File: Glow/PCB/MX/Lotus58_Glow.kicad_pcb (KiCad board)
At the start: 2 copper layers, 139.1 x 107.7 mm, 122 parts, among them J1 AudioJack4, P4 OLED, SW1 SW_PUSH, SW10 SW_PUSH, SW11 SW_PUSH, SW12 SW_PUSH, SW13 SW_PUSH, SW14 SW_PUSH, SW15 SW_PUSH, SW16 SW_PUSH, SW17 SW_PUSH, SW18 SW_PUSH, SW19 SW_PUSH, SW2 SW_PUSH, SW20 SW_PUSH, SW21 SW_PUSH, SW22 SW_PUSH, SW23 SW_PUSH, SW24 SW_PUSH, SW25 SW_PUSH, SW26 SW_PUSH, SW27 SW_PUSH, SW28 SW_PUSH, SW29 SW_PUSH, SW3 SW_PUSH, SW30 Rotary_Encoder_Switch, SW31 Rotary_Encoder_Switch, SW4 SW_PUSH, SW5 SW_PUSH, SW6 SW_PUSH, SW7 SW_PUSH, SW8 SW_PUSH, SW9 SW_PUSH, U1 ProMicro

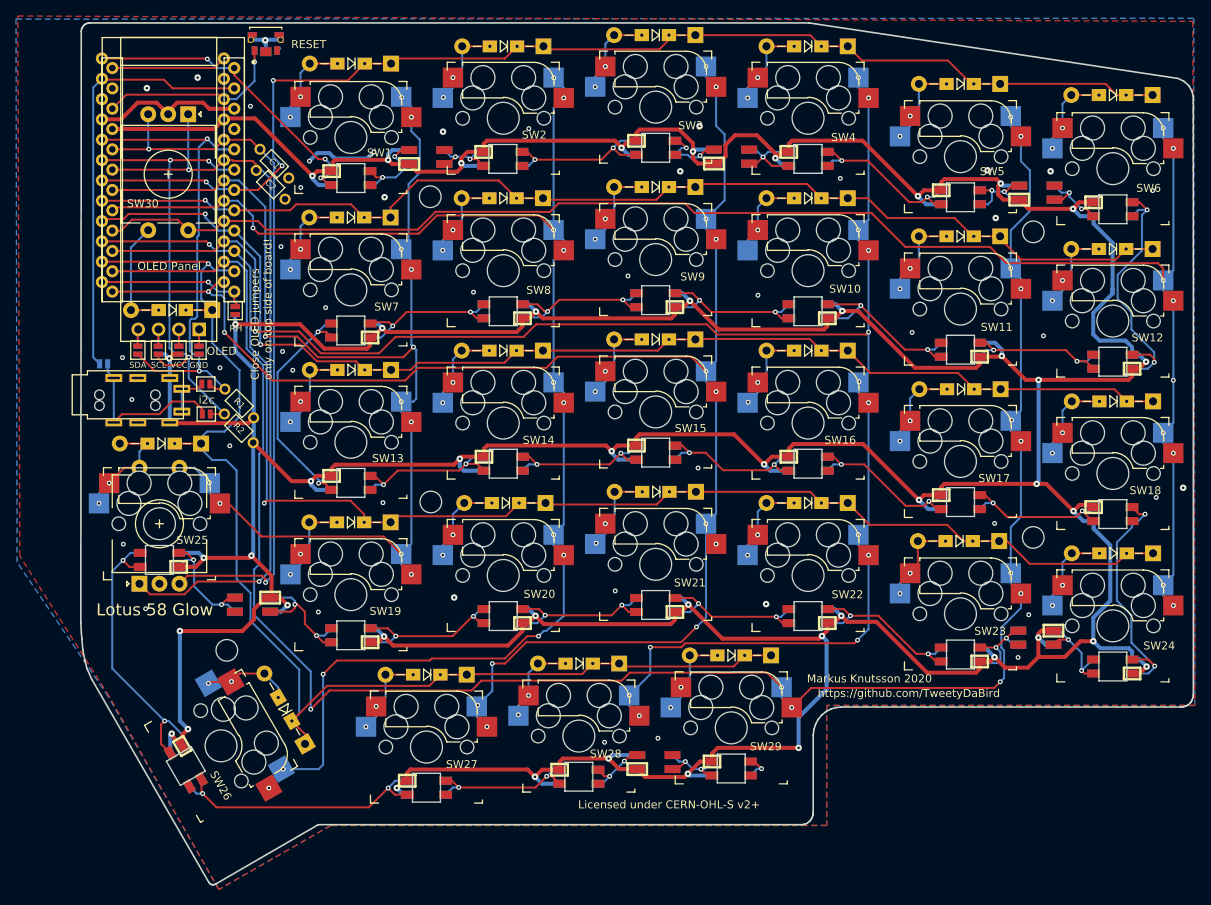
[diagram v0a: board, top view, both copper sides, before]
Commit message: RGB midmount footprints
Fixed mirror image pinout
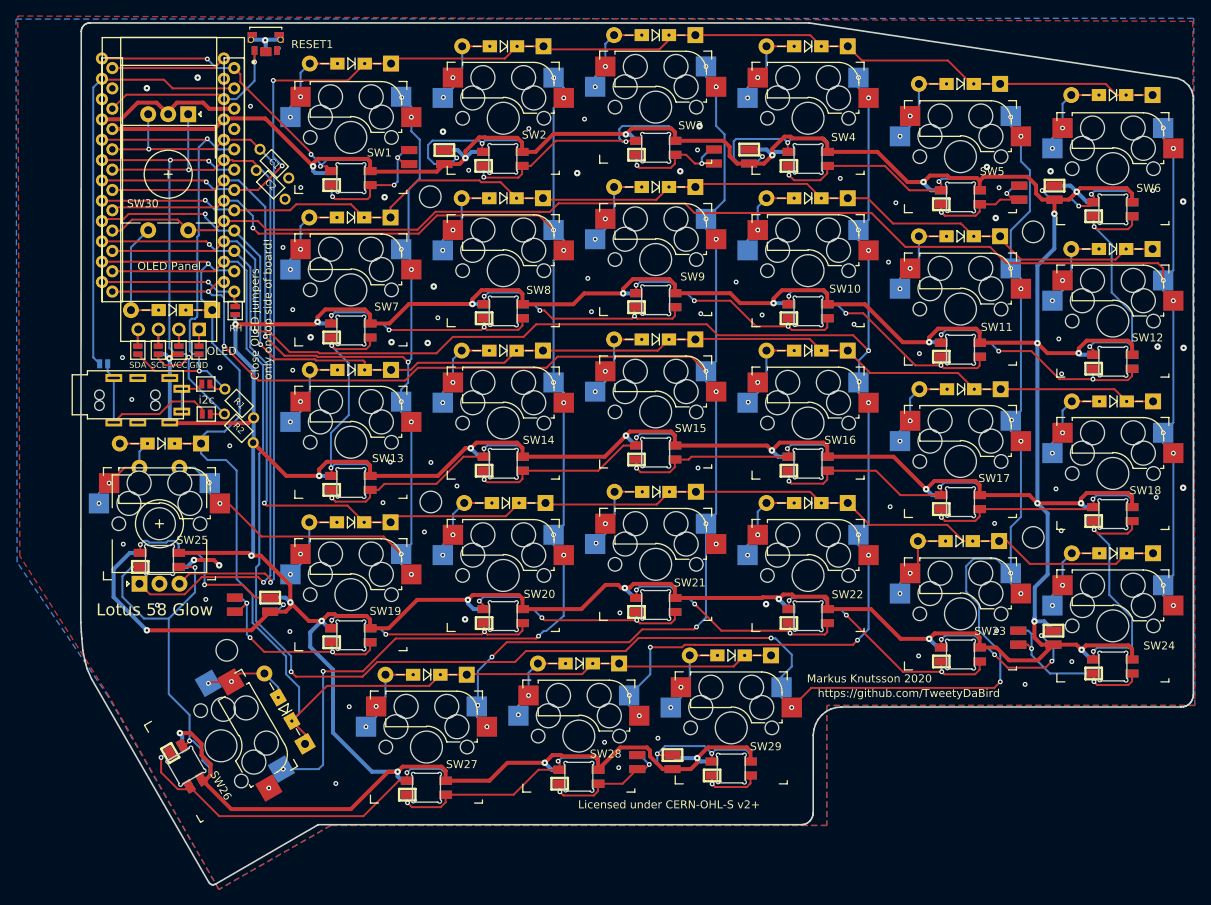
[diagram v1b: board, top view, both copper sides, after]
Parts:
- turned L1 to 0 degrees
- turned L13 to 0 degrees
- turned L14 to 0 degrees
- turned L15 to 0 degrees
- turned L16 to 0 degrees
- turned L17 to 0 degrees
- turned L18 to 0 degrees
- turned L26 to 300 degrees
- turned L27 to 0 degrees
- turned L28 to 0 degrees
- turned L29 to 0 degrees
- turned L3 to 0 degrees
- turned L31 to 0 degrees
- turned L33 to 0 degrees
- turned L34 to 0 degrees
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- renumbered RESET to RESET1
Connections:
- L1 pad 1: Net-(L1-Pad1) -> GND
- L1 pad 2: GND -> LED
- L1 pad 3: LED -> VCC
- L1 pad 4: VCC -> Net-(L1-Pad4)
- L10 pad 1: Net-(L10-Pad1) -> GND
- L10 pad 2: GND -> Net-(L10-Pad2)
- L10 pad 3: Net-(L10-Pad3) -> VCC
- L10 pad 4: VCC -> Net-(L10-Pad4)
- L11 pad 1: Net-(L10-Pad3) -> GND
- L11 pad 2: GND -> Net-(L11-Pad2)
- L11 pad 3: Net-(L11-Pad3) -> VCC
- L11 pad 4: VCC -> Net-(L10-Pad2)
- L12 pad 1: Net-(L11-Pad3) -> GND
- L12 pad 2: GND -> Net-(L12-Pad2)
- L12 pad 3: Net-(L12-Pad3) -> VCC
- L12 pad 4: VCC -> Net-(L11-Pad2)
- L13 pad 1: Net-(L13-Pad1) -> GND
- L13 pad 2: GND -> Net-(L13-Pad2)
- L13 pad 3: Net-(L13-Pad3) -> VCC
- L13 pad 4: VCC -> Net-(L13-Pad4)
- L14 pad 1: Net-(L14-Pad1) -> GND
- L14 pad 2: GND -> Net-(L13-Pad4)
- L14 pad 3: Net-(L13-Pad1) -> VCC
- L14 pad 4: VCC -> Net-(L14-Pad4)
- L15 pad 1: Net-(L15-Pad1) -> GND
- L15 pad 2: GND -> Net-(L14-Pad4)
- L15 pad 3: Net-(L14-Pad1) -> VCC
- L15 pad 4: VCC -> Net-(L15-Pad4)
- L16 pad 1: Net-(L16-Pad1) -> GND
- L16 pad 2: GND -> Net-(L15-Pad4)
- L16 pad 3: Net-(L15-Pad1) -> VCC
- L16 pad 4: VCC -> Net-(L16-Pad4)
- L17 pad 1: Net-(L17-Pad1) -> GND
- L17 pad 2: GND -> Net-(L16-Pad4)
- L17 pad 3: Net-(L16-Pad1) -> VCC
- L17 pad 4: VCC -> Net-(L17-Pad4)
- L18 pad 1: Net-(L18-Pad1) -> GND
- L18 pad 2: GND -> Net-(L17-Pad4)
- L18 pad 3: Net-(L17-Pad1) -> VCC
- L18 pad 4: VCC -> Net-(L18-Pad4)
- L19 pad 1: Net-(L19-Pad1) -> GND
- L19 pad 2: GND -> Net-(L19-Pad2)
- L19 pad 3: Net-(L19-Pad3) -> VCC
- L19 pad 4: VCC -> Net-(L19-Pad4)
- L2 pad 1: Net-(L2-Pad1) -> GND
- L2 pad 2: GND -> Net-(L2-Pad2)
- L2 pad 3: Net-(L2-Pad3) -> VCC
- L2 pad 4: VCC -> Net-(L2-Pad4)
- L20 pad 1: Net-(L19-Pad3) -> GND
- L20 pad 2: GND -> Net-(L20-Pad2)
- L20 pad 3: Net-(L20-Pad3) -> VCC
- L20 pad 4: VCC -> Net-(L19-Pad2)
- L21 pad 1: Net-(L20-Pad3) -> GND
- L21 pad 2: GND -> Net-(L21-Pad2)
- L21 pad 3: Net-(L21-Pad3) -> VCC
- L21 pad 4: VCC -> Net-(L20-Pad2)
- L22 pad 1: Net-(L21-Pad3) -> GND
- L22 pad 2: GND -> Net-(L22-Pad2)
- L22 pad 3: Net-(L22-Pad3) -> VCC
- L22 pad 4: VCC -> Net-(L21-Pad2)
- L23 pad 1: Net-(L22-Pad3) -> GND
- L23 pad 2: GND -> Net-(L23-Pad2)
- L23 pad 3: Net-(L23-Pad3) -> VCC
- L23 pad 4: VCC -> Net-(L22-Pad2)
- L24 pad 1: Net-(L24-Pad1) -> GND
- L24 pad 2: GND -> Net-(L18-Pad4)
- L24 pad 3: Net-(L18-Pad1) -> VCC
- L24 pad 4: VCC -> Net-(L24-Pad4)
- L25 pad 1: Net-(L25-Pad1) -> GND
- L25 pad 2: GND -> Net-(L25-Pad2)
- L25 pad 3: Net-(L25-Pad3) -> VCC
- L25 pad 4: VCC -> Net-(L25-Pad4)
- L26 pad 1: Net-(L26-Pad1) -> GND
- L26 pad 2: GND -> Net-(L25-Pad4)
- L26 pad 3: Net-(L25-Pad1) -> VCC
- L26 pad 4: VCC -> Net-(L26-Pad4)
- L27 pad 1: Net-(L27-Pad1) -> GND
- L27 pad 2: GND -> Net-(L26-Pad4)
- L27 pad 3: Net-(L26-Pad1) -> VCC
- L27 pad 4: VCC -> Net-(L27-Pad4)
- L28 pad 1: Net-(L28-Pad1) -> GND
- L28 pad 2: GND -> Net-(L27-Pad4)
- L28 pad 3: Net-(L27-Pad1) -> VCC
- L28 pad 4: VCC -> Net-(L28-Pad4)
- L29 pad 1: Net-(L29-Pad1) -> GND
- L29 pad 2: GND -> Net-(L29-Pad2)
- L29 pad 3: Net-(L29-Pad3) -> VCC
- L29 pad 4: VCC -> Net-(L29-Pad4)
- L3 pad 1: Net-(L3-Pad1) -> GND
- L3 pad 2: GND -> Net-(L2-Pad4)
- L3 pad 3: Net-(L2-Pad1) -> VCC
- L3 pad 4: VCC -> Net-(L3-Pad4)
- L30 pad 1: Net-(L23-Pad3) -> GND
- L30 pad 2: GND -> Net-(L24-Pad4)
- L30 pad 3: Net-(L24-Pad1) -> VCC
- L30 pad 4: VCC -> Net-(L23-Pad2)
- L31 pad 1: Net-(L29-Pad3) -> GND
- L31 pad 2: GND -> Net-(L28-Pad4)
- L31 pad 3: Net-(L28-Pad1) -> VCC
- L31 pad 4: VCC -> Net-(L29-Pad2)
- L32 pad 1: Net-(L25-Pad3) -> GND
- L32 pad 2: GND -> Net-(L19-Pad4)
- L32 pad 3: Net-(L19-Pad1) -> VCC
- L32 pad 4: VCC -> Net-(L25-Pad2)
- L33 pad 1: Net-(L33-Pad1) -> GND
- L33 pad 2: GND -> Net-(L33-Pad2)
- L33 pad 3: Net-(L33-Pad3) -> VCC
- L33 pad 4: VCC -> Net-(L33-Pad4)
- L34 pad 1: Net-(L34-Pad1) -> GND
- L34 pad 2: GND -> Net-(L3-Pad4)
- L34 pad 3: Net-(L3-Pad1) -> VCC
- L34 pad 4: VCC -> Net-(L34-Pad4)
- L35 pad 1: Net-(L2-Pad3) -> GND
- L35 pad 2: GND -> Net-(L1-Pad4)
- L35 pad 3: Net-(L1-Pad1) -> VCC
- L35 pad 4: VCC -> Net-(L2-Pad2)
- L4 pad 1: Net-(L4-Pad1) -> GND
- L4 pad 2: GND -> Net-(L34-Pad4)
- L4 pad 3: Net-(L34-Pad1) -> VCC
- L4 pad 4: VCC -> Net-(L4-Pad4)
- L5 pad 1: Net-(L33-Pad3) -> GND
- L5 pad 2: GND -> Net-(L4-Pad4)
- L5 pad 3: Net-(L4-Pad1) -> VCC
- L5 pad 4: VCC -> Net-(L33-Pad2)
- L6 pad 1: Net-(L12-Pad3) -> GND
- L6 pad 2: GND -> Net-(L33-Pad4)
- L6 pad 3: Net-(L33-Pad1) -> VCC
- L6 pad 4: VCC -> Net-(L12-Pad2)
- L7 pad 1: Net-(L13-Pad3) -> GND
- L7 pad 2: GND -> Net-(L7-Pad2)
- L7 pad 3: Net-(L7-Pad3) -> VCC
- L7 pad 4: VCC -> Net-(L13-Pad2)
- L8 pad 1: Net-(L7-Pad3) -> GND
- L8 pad 2: GND -> Net-(L8-Pad2)
- L8 pad 3: Net-(L8-Pad3) -> VCC
- L8 pad 4: VCC -> Net-(L7-Pad2)
- L9 pad 1: Net-(L8-Pad3) -> GND
- L9 pad 2: GND -> Net-(L10-Pad4)
- L9 pad 3: Net-(L10-Pad1) -> VCC
- L9 pad 4: VCC -> Net-(L8-Pad2)
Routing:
- net VCC: track 843.5 -> 890.8 mm, vias 45 -> 37
- net Net-(L25-Pad4): track 0.00 -> 46.4 mm, vias 0 -> 2
- net Net-(L26-Pad4): track 0.00 -> 45.6 mm, vias 0 -> 2
- net Net-(L25-Pad1): track 37.4 -> 0.00 mm, vias 2 -> 0
- net Net-(L26-Pad1): track 34.3 -> 0.00 mm, vias 2 -> 0
- net Net-(L2-Pad4): track 0.00 -> 33.7 mm, vias 0 -> 2
- net Net-(L12-Pad3): track 33.5 -> 0.00 mm, vias 2 -> 0
- net Net-(L12-Pad2): track 0.00 -> 33.4 mm, vias 0 -> 2
- net Net-(L10-Pad2): track 0.00 -> 32.3 mm, vias 0 -> 3
- net Net-(L22-Pad2): track 0.00 -> 32.1 mm, vias 0 -> 3
- net Net-(L18-Pad4): track 0.00 -> 31.7 mm, vias 0 -> 2
- net Net-(L13-Pad2): track 0.00 -> 31.6 mm, vias 0 -> 2
- net Net-(L18-Pad1): track 31.3 -> 0.00 mm, vias 2 -> 0
- net Net-(L13-Pad3): track 31.3 -> 0.00 mm, vias 2 -> 0
- net Net-(L4-Pad4): track 0.00 -> 30.8 mm, vias 0 -> 2
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
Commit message: Component values/BOM added
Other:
- rule pad_to_mask_clearance: 0.2 -> 0
